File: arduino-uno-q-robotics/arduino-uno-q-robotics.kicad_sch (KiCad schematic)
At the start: 19 parts, among them J1 Conn_02x30_Odd_Even, J2 Conn_02x30_Odd_Even, J3 Connector_FFC-FPC, J4 Connector_FFC-FPC, J5 Conn_02x13_Odd_Even, J6 Conn_02x04_Odd_Even, U1 LSM6DSO32, U2 TCA9803, U4 TCA9803

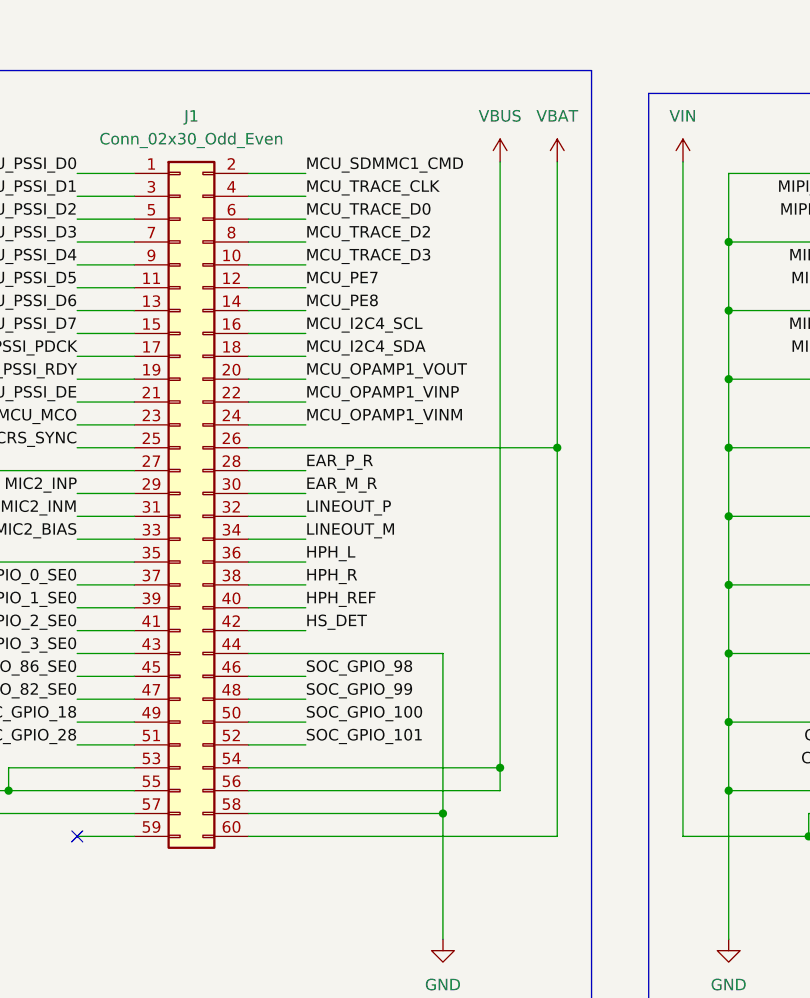
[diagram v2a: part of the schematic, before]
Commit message: Fix DRC warnings/errors
Fix DRC errors
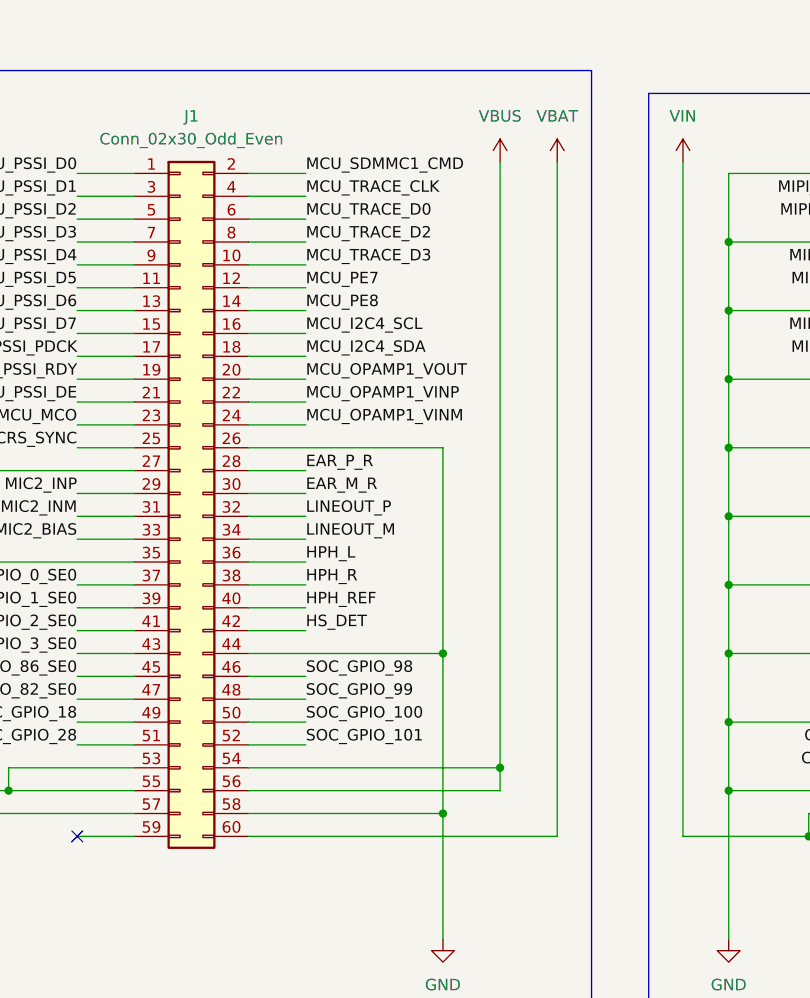
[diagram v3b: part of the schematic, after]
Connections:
- net GND: now also J1.26 (Pin_26)
- net VBAT: no longer J1.26 (Pin_26)
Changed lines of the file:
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@@
+	)
+	(junction
+		(at 93.98 85.09)
+		(diameter 0)
+		(color 0 0 0 0)
 	)
 	(junction
@@
 	(junction
 		(at 134.62 105.41)
-		(diameter 0)
-		(color 0 0 0 0)
-	)
-	(junction
-		(at 106.68 62.23)
 		(diameter 0)
 		(color 0 0 0 0)
@@
 	(wire
 		(pts
-			(xy 106.68 62.23) (xy 106.68 30.48)
-		)
-		(stroke
-			(width 0)
-			(type default)
-		)
-	)
-	(wire
-		(pts
 			(xy 381 88.9) (xy 363.22 88.9)
 		)
@@
 	(wire
 		(pts
+			(xy 93.98 62.23) (xy 93.98 85.09)
+		)
+		(stroke
+			(width 0)
+			(type default)
+		)
+	)
+	(wire
+		(pts
 			(xy 104.14 140.97) (xy 109.22 140.97)
 		)
@@
 	(wire
 		(pts
+			(xy 93.98 85.09) (xy 93.98 102.87)
+		)
+		(stroke
+			(width 0)
+			(type default)
+		)
+	)
+	(wire
+		(pts
 			(xy 78.74 92.71) (xy 72.39 92.71)
 		)
@@
 	(wire
 		(pts
+			(xy 72.39 62.23) (xy 93.98 62.23)
+		)
+		(stroke
+			(width 0)
+			(type default)
+		)
+	)
+	(wire
+		(pts
 			(xy 78.74 69.85) (xy 72.39 69.85)
 		)
@@
 	(wire
 		(pts
-			(xy 72.39 62.23) (xy 106.68 62.23)
-		)
-		(stroke
-			(width 0)
-			(type default)
-		)
-	)
-	(wire
-		(pts
 			(xy 302.26 104.14) (xy 309.88 104.14)
 		)
@@
 	(wire
 		(pts
-			(xy 106.68 105.41) (xy 106.68 62.23)
+			(xy 106.68 30.48) (xy 106.68 105.41)
 		)
 		(stroke
@@
 		)
 		(stroke
-			(width 0)
-			(type default)
-		)
-	)
-	(wire
-		(pts
-			(xy 93.98 85.09) (xy 93.98 102.87)
-		)
-		(stroke

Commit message: Organize schematic sheet
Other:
- note added: "Gyro/Acce Sensor"
- note added: "I2C Pullup Resistors"
- note added: "JMISC/MEDIA Breakout Headers"
- note added: "STEMMA Port"
- moved on the sheet: C3, C4, J6, R3, U1, U3

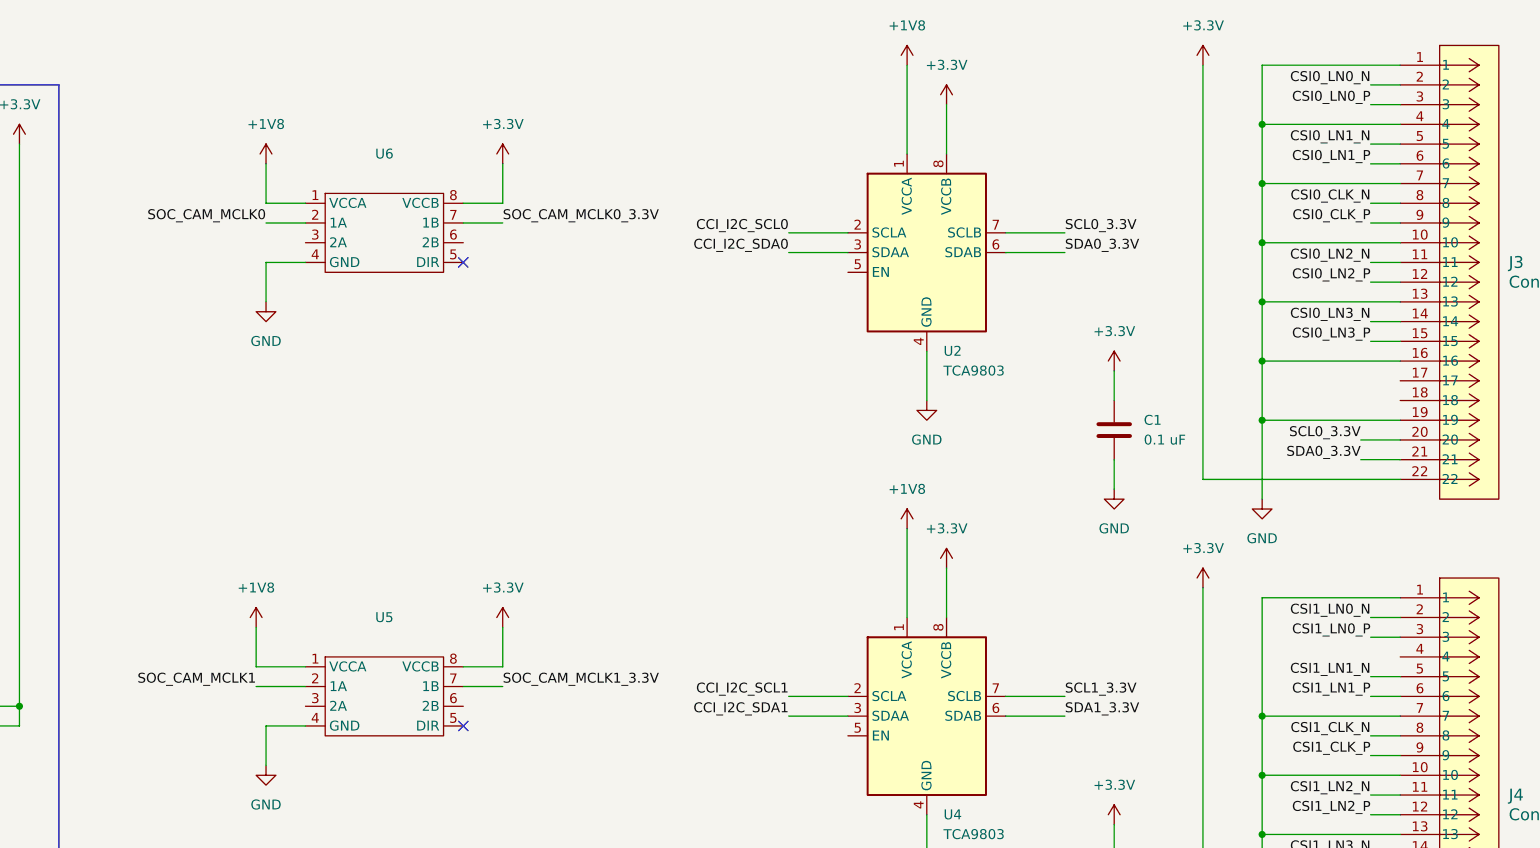
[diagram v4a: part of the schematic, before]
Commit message: Adjust MCLK traces/vias
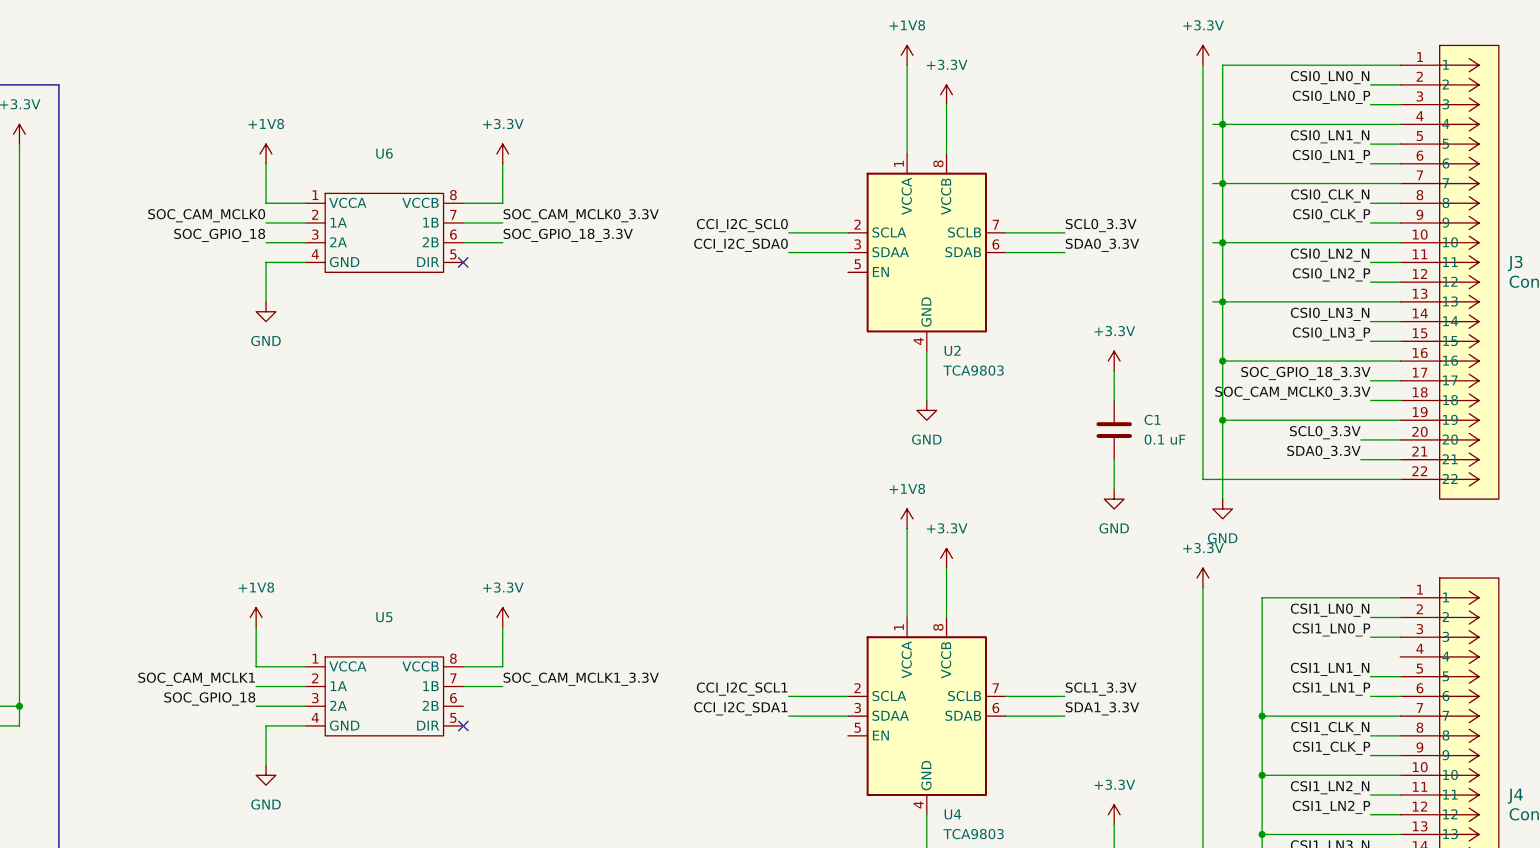
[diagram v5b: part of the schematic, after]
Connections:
- net SOC_CAM_MCLK0_3.3V: now also J3.18
- net SOC_GPIO_18: now also U5.3 (2A), U6.3 (2A)
- net SOC_GPIO_18_3.3V: now reaches U6.6 (2B)
- net SOC_GPIO_18_3.3V: now also J3.17

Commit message: Move placement of camera components
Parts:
- removed J5: Conn_02x13_Odd_Even, Connector_PinSocket_2.54mm:PinSocket_2x13_P2.54mm_Vertical_SMD, symbol Connector_Generic:Conn_02x13_Odd_Even
- removed J6: Conn_02x04_Odd_Even, Connector_PinHeader_2.54mm:PinHeader_2x04_P2.54mm_Vertical_SMD, symbol Connector_Generic:Conn_02x04_Odd_Even
- removed R3: 10k, Resistor_SMD:R_0603_1608Metric_Pad0.98x0.95mm_HandSolder, symbol Device:R
- added J5: Conn_02x30_Odd_Even, Connector_PinSocket_1.27mm:PinSocket_2x30_P1.27mm_Vertical_SMD, symbol Connector_Generic:Conn_02x30_Odd_Even
- J2: footprint Connector_PinHeader_1.27mm:PinHeader_2x30_P1.27mm_Vertical -> Connector_PinHeader_1.27mm:PinHeader_2x30_P1.27mm_Vertical_SMD
- U3: footprint Connector_JST:JST_SH_SM04B-SRSS-TB_1x04-1MP_P1.00mm_Horizontal -> Connector_JST:JST_SH_BM04B-SRSS-TB_1x04-1MP_P1.00mm_Vertical
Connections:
- net +1V8: now also J5.57 (Pin_57)
- net +3.3V: now also J5.53 (Pin_53), J5.55 (Pin_55)
- net EAR_M_R: now also J5.30 (Pin_30)
- net EAR_P_R: now also J5.28 (Pin_28)
- net GND: now also J5.26 (Pin_26), J5.27 (Pin_27), J5.35 (Pin_35), J5.44 (Pin_44), J5.58 (Pin_58)
- net HPH_L: now also J5.36 (Pin_36)
- net HPH_R: now also J5.38 (Pin_38)
- net HPH_REF: now also J5.40 (Pin_40)
- net HS_DET: now also J5.42 (Pin_42)
- net LINEOUT_M: now also J5.34 (Pin_34)
- net LINEOUT_P: now also J5.32 (Pin_32)
- net MCU_CRS_SYNC: now also J5.25 (Pin_25)
- net MCU_I2C4_SCL: now also J5.16 (Pin_16)
- net MCU_I2C4_SDA: now also J5.18 (Pin_18)
- net MCU_MCO: now also J5.23 (Pin_23)
- net MCU_OPAMP1_VINM: now also J5.24 (Pin_24)
- net MCU_OPAMP1_VINP: now also J5.22 (Pin_22)
- net MCU_OPAMP1_VOUT: now also J5.20 (Pin_20)
- net MCU_PE7: now also J5.12 (Pin_12)
- net MCU_PE8: now also J5.14 (Pin_14)
- net MCU_PSSI_D0: now also J5.1 (Pin_1)
- net MCU_PSSI_D1: now also J5.3 (Pin_3)
- net MCU_PSSI_D2: now also J5.5 (Pin_5)
- net MCU_PSSI_D3: now also J5.7 (Pin_7)
- net MCU_PSSI_D4: now also J5.9 (Pin_9)
- net MCU_PSSI_D5: now also J5.11 (Pin_11)
- net MCU_PSSI_D6: now also J5.13 (Pin_13)
- net MCU_PSSI_D7: now also J5.15 (Pin_15)
- net MCU_PSSI_DE: now also J5.21 (Pin_21)
- net MCU_PSSI_PDCK: now also J5.17 (Pin_17)
- net MCU_PSSI_RDY: now also J5.19 (Pin_19)
- net MCU_SDMMC1_CMD: now also J5.2 (Pin_2)
- net MCU_TRACE_CLK: now also J5.4 (Pin_4)
- net MCU_TRACE_D0: now also J5.6 (Pin_6)
- net MCU_TRACE_D2: now also J5.8 (Pin_8)
- net MCU_TRACE_D3: now also J5.10 (Pin_10)
- net MIC2_BIAS: now also J5.33 (Pin_33)
- net MIC2_INM: now also J5.31 (Pin_31)
- net MIC2_INP: now also J5.29 (Pin_29)
- net SOC_GPIO_0_SE0: now also J5.37 (Pin_37)
- net SOC_GPIO_100: now also J5.50 (Pin_50)
- net SOC_GPIO_101: now also J5.52 (Pin_52)
- net SOC_GPIO_18: now also J5.49 (Pin_49)
- net SOC_GPIO_1_SE0: now also J5.39 (Pin_39)
- net SOC_GPIO_28: now also J5.51 (Pin_51)
- net SOC_GPIO_2_SE0: now also J5.41 (Pin_41)
- net SOC_GPIO_3_SE0: now also J5.43 (Pin_43)
- net SOC_GPIO_82_SE0: now also J5.47 (Pin_47)
- net SOC_GPIO_86_SE0: now also J5.45 (Pin_45)
- net SOC_GPIO_98: now also J5.46 (Pin_46)
- net SOC_GPIO_99: now also J5.48 (Pin_48)
- net VBAT: now also J5.60 (Pin_60)
- net VBUS: now also J5.54 (Pin_54), J5.56 (Pin_56)
- net CS: no longer names the net of U1.12 (CS)
- no-connect marks 8 -> 10
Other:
- note added: "Camera Connectors"
- note added: "JMISC Top Layer"
- note added: "ONLY FOR PROTOTYPE"
- note added: "T"
- note removed: "JMISC/MEDIA Breakout Headers"
- moved on the sheet: C2, C3, J4, U3, U4, U5
